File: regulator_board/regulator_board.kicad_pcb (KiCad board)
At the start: 2 copper layers, 125.7 x 35.6 mm, 73 parts, among them J1 BATT, J10 5VOUT, J11 9VOUT, J12 9VOUT, J13 9VOUT, J2 5VOUT, J3 5VOUT, J4 5VOUT, J5 5VOUT, J6 5VOUT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

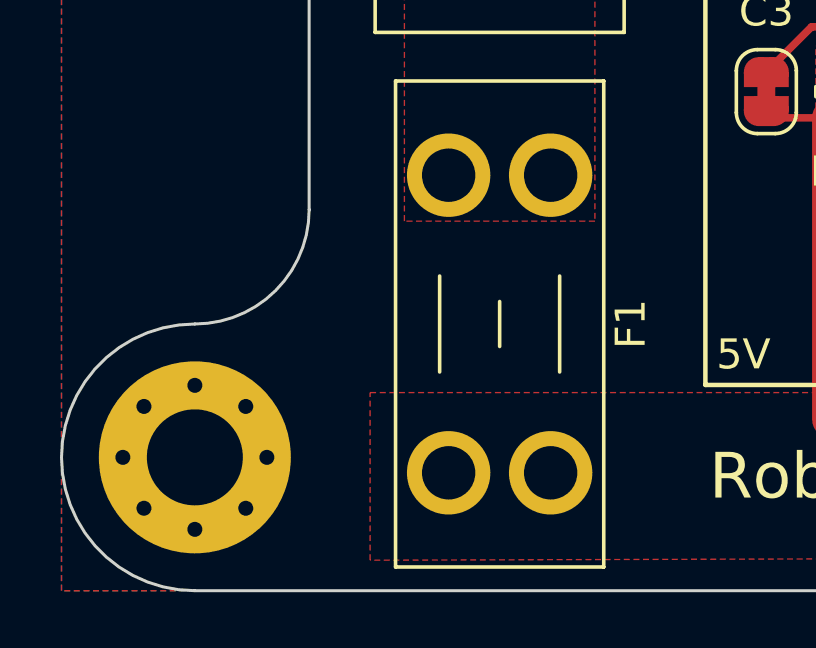
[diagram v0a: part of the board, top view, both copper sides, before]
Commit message: add order number position
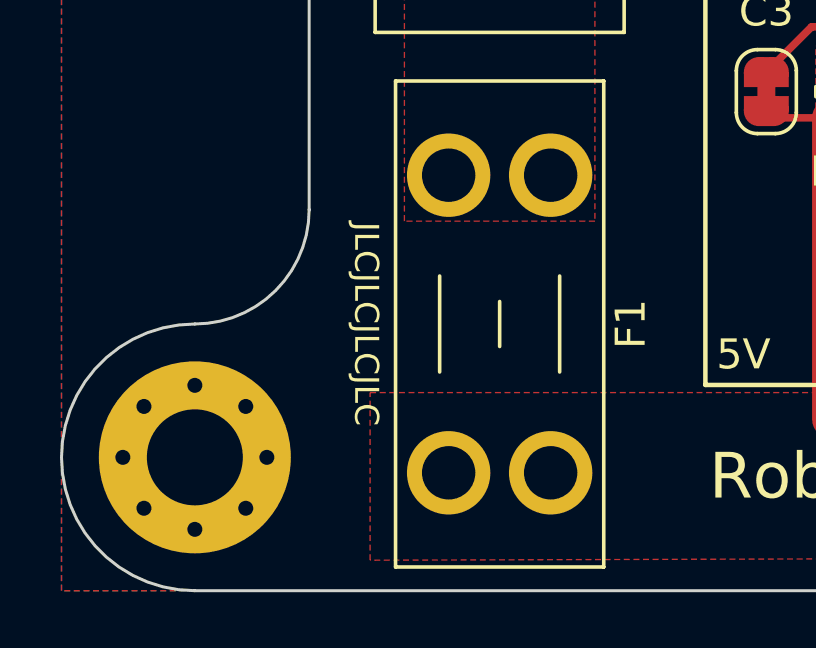
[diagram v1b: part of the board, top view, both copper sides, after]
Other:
- board text added: "JLCJLCJLCJLC"
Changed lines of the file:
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@@
     (effects (font (size 1.524 1.524) (thickness 0.254)) (justify left))
+  )
+  (gr_text "JLCJLCJLCJLC" (at 60.325 143.51 270) (layer "F.SilkS")
+    (effects (font (size 0.8 0.8) (thickness 0.15)))
   )
   (gr_text "5V" (at 72.898 144.526) (layer "F.SilkS")
